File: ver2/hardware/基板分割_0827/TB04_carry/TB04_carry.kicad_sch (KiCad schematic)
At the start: 7 parts, among them J1602 Screw_Terminal_01x02, U102 74HC138

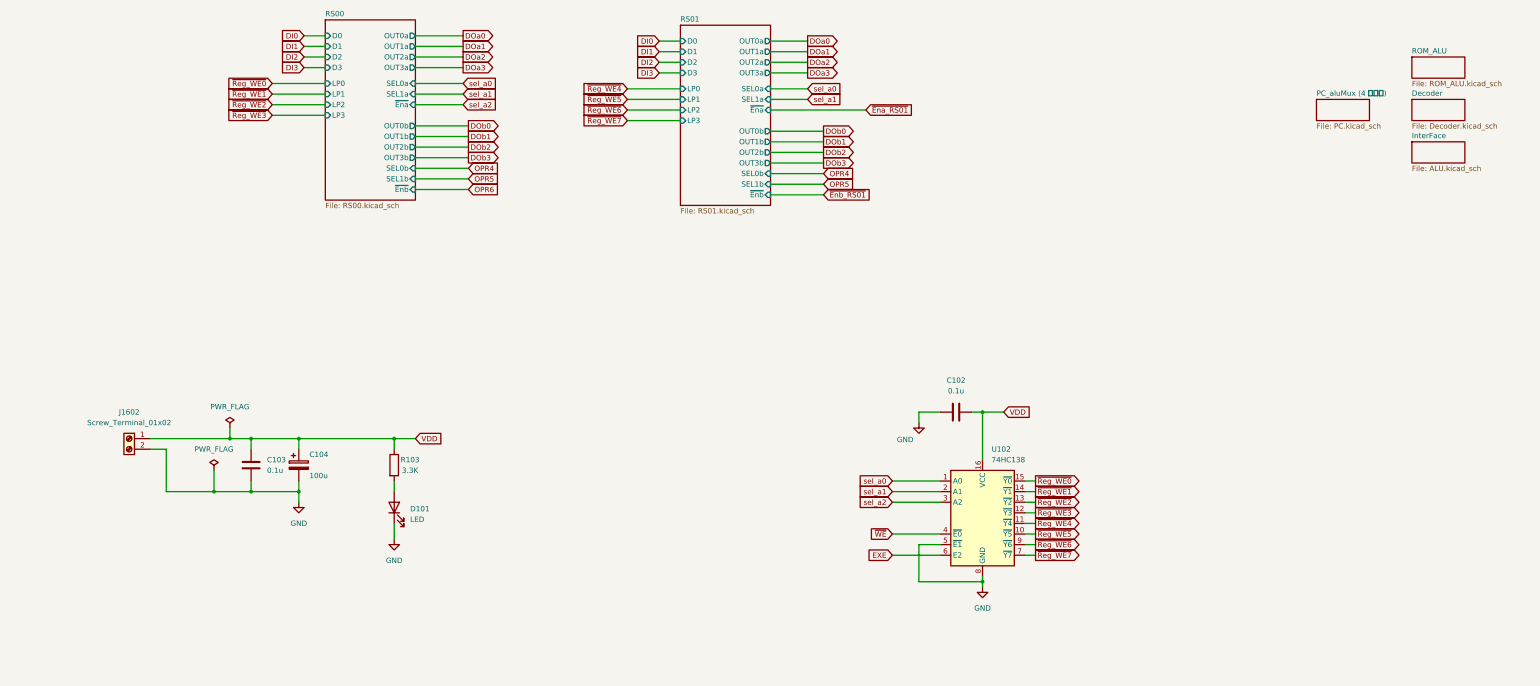
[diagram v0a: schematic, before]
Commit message: ver2: 3分割でシート内の不要部品・配線を削除(検証合格)／キャリアを0827へコピー
- 制御34・演算25・IF10=IC69でマスターと一致、部品の取りこぼし0
- ピン-ネット署名の変化0件=誤って線を切った箇所なし
- またぐ信号は制御/演算35・IF/制御18で手順書の表と過不足ゼロ

Co-Authored-By: Claude Opus 5 <noreply@anthropic.com>
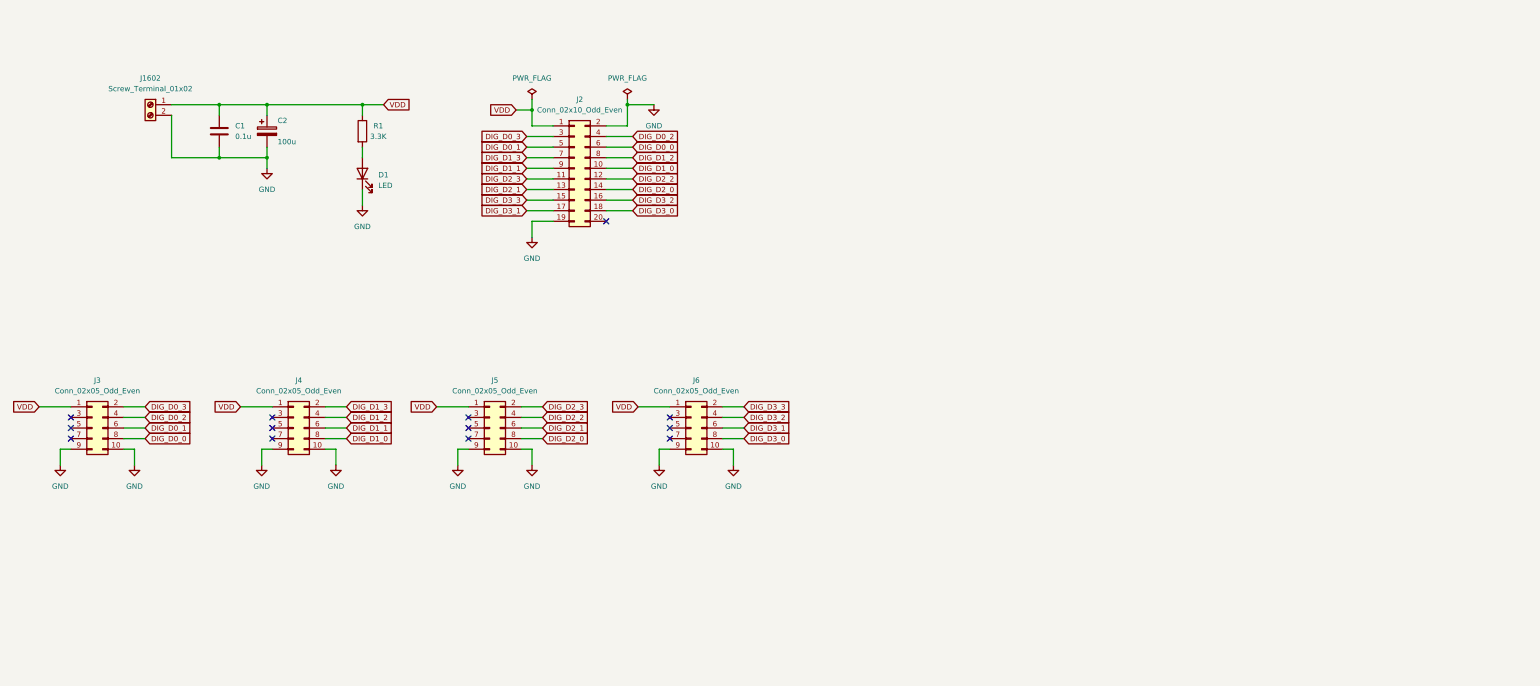
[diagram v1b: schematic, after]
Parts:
- removed C102: 0.1u, Capacitor_THT:C_Disc_D4.3mm_W1.9mm_P5.00mm, symbol Device:C
- removed U102: 74HC138, Package_DIP:DIP-16_W7.62mm_Socket, symbol 74xx:74HC138
- added J2: Conn_02x10_Odd_Even, Connector_PinSocket_2.54mm:PinSocket_2x10_P2.54mm_Vertical, symbol Connector_Generic:Conn_02x10_Odd_Even
- added J3, J4, J5, J6: Conn_02x05_Odd_Even, Connector_PinSocket_2.54mm:PinSocket_2x05_P2.54mm_Vertical, symbol Connector_Generic:Conn_02x05_Odd_Even
- J1602: footprint (none) -> TerminalBlock:TerminalBlock_MaiXu_MX126-5.0-02P_1x02_P5.00mm
- renumbered C103 to C1, C104 to C2, D101 to D1, R103 to R1
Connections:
- net GND: now also J2.19 (Pin_19), J2.2 (Pin_2), J3.10 (Pin_10), J3.9 (Pin_9), J4.10 (Pin_10), J4.9 (Pin_9), J5.10 (Pin_10), J5.9 (Pin_9), J6.10 (Pin_10), J6.9 (Pin_9)
- net VDD: now also J2.1 (Pin_1), J3.1 (Pin_1), J4.1 (Pin_1), J5.1 (Pin_1), J6.1 (Pin_1)
- new net DIG_D0_0: J2.6 (Pin_6), J3.8 (Pin_8)
- new net DIG_D0_1: J2.5 (Pin_5), J3.6 (Pin_6)
- new net DIG_D0_2: J2.4 (Pin_4), J3.4 (Pin_4)
- new net DIG_D0_3: J2.3 (Pin_3), J3.2 (Pin_2)
- new net DIG_D1_0: J2.10 (Pin_10), J4.8 (Pin_8)
- new net DIG_D1_1: J2.9 (Pin_9), J4.6 (Pin_6)
- new net DIG_D1_2: J2.8 (Pin_8), J4.4 (Pin_4)
- new net DIG_D1_3: J2.7 (Pin_7), J4.2 (Pin_2)
- new net DIG_D2_0: J2.14 (Pin_14), J5.8 (Pin_8)
- new net DIG_D2_1: J2.13 (Pin_13), J5.6 (Pin_6)
- new net DIG_D2_2: J2.12 (Pin_12), J5.4 (Pin_4)
- new net DIG_D2_3: J2.11 (Pin_11), J5.2 (Pin_2)
- new net DIG_D3_0: J2.18 (Pin_18), J6.8 (Pin_8)
- new net DIG_D3_1: J2.17 (Pin_17), J6.6 (Pin_6)
- new net DIG_D3_2: J2.16 (Pin_16), J6.4 (Pin_4)
- new net DIG_D3_3: J2.15 (Pin_15), J6.2 (Pin_2)
- no-connect marks 0 -> 13
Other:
- removed sheet Decoder
- removed sheet InterFace
- removed sheet PC_aluMux (4 ページ)
- removed sheet ROM_ALU
- removed sheet RS00
- removed sheet RS01
- moved on the sheet: C1, C2, D1, R1

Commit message: ver2: 3分割のフットプリント設定完了・取付穴を追加・PCBを作り直し
- 新規コネクタ11件のフットプリントを設定(2x20/2x10ピンソケット・端子台)
- 演算板/制御板/キャリアに取付穴MountingHole_Pad×4とGNDを追加(M3・パッド付きビア)
- 3枚のPCBをコピー元マスターのレイアウトを一掃して作り直し(配置前・配線0)
- 階層から外れて残っていたRS00/RS01.kicad_sch(制御板・IF板)を削除

検証: フットプリント未設定0件、回路図とPCBの参照番号の集合差分0
(演算102/制御101/IF127/キャリア14)、回路図の電気的変更なし

Co-Authored-By: Claude Opus 5 <noreply@anthropic.com>
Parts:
- added H1, H2, H3, H4: MountingHole_Pad, MountingHole:MountingHole_3.2mm_M3_Pad_Via, symbol Mechanical:MountingHole_Pad
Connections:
- net GND: now also H1.1, H2.1, H3.1, H4.1
